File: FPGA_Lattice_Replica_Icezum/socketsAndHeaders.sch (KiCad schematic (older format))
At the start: 39 parts, among them J10 1x8_male_pin_Header_2.54mm, J11 1x6_female_pin_Header_2.54mm, J12 1x6_female_pin_Header_2.54mm, J13 1x6_female_pin_Header_2.54mm, J14 1x6_female_pin_Header_2.54mm, J19 2x4_male_pin_Header_2.54mm, J2 1x6_female_pin_Header_2.54mm, J3 1x6_female_pin_Header_2.54mm, J4 1x10_female_pin_Header_2.54mm, J5 1x8_male_pin_Header_2.54mm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

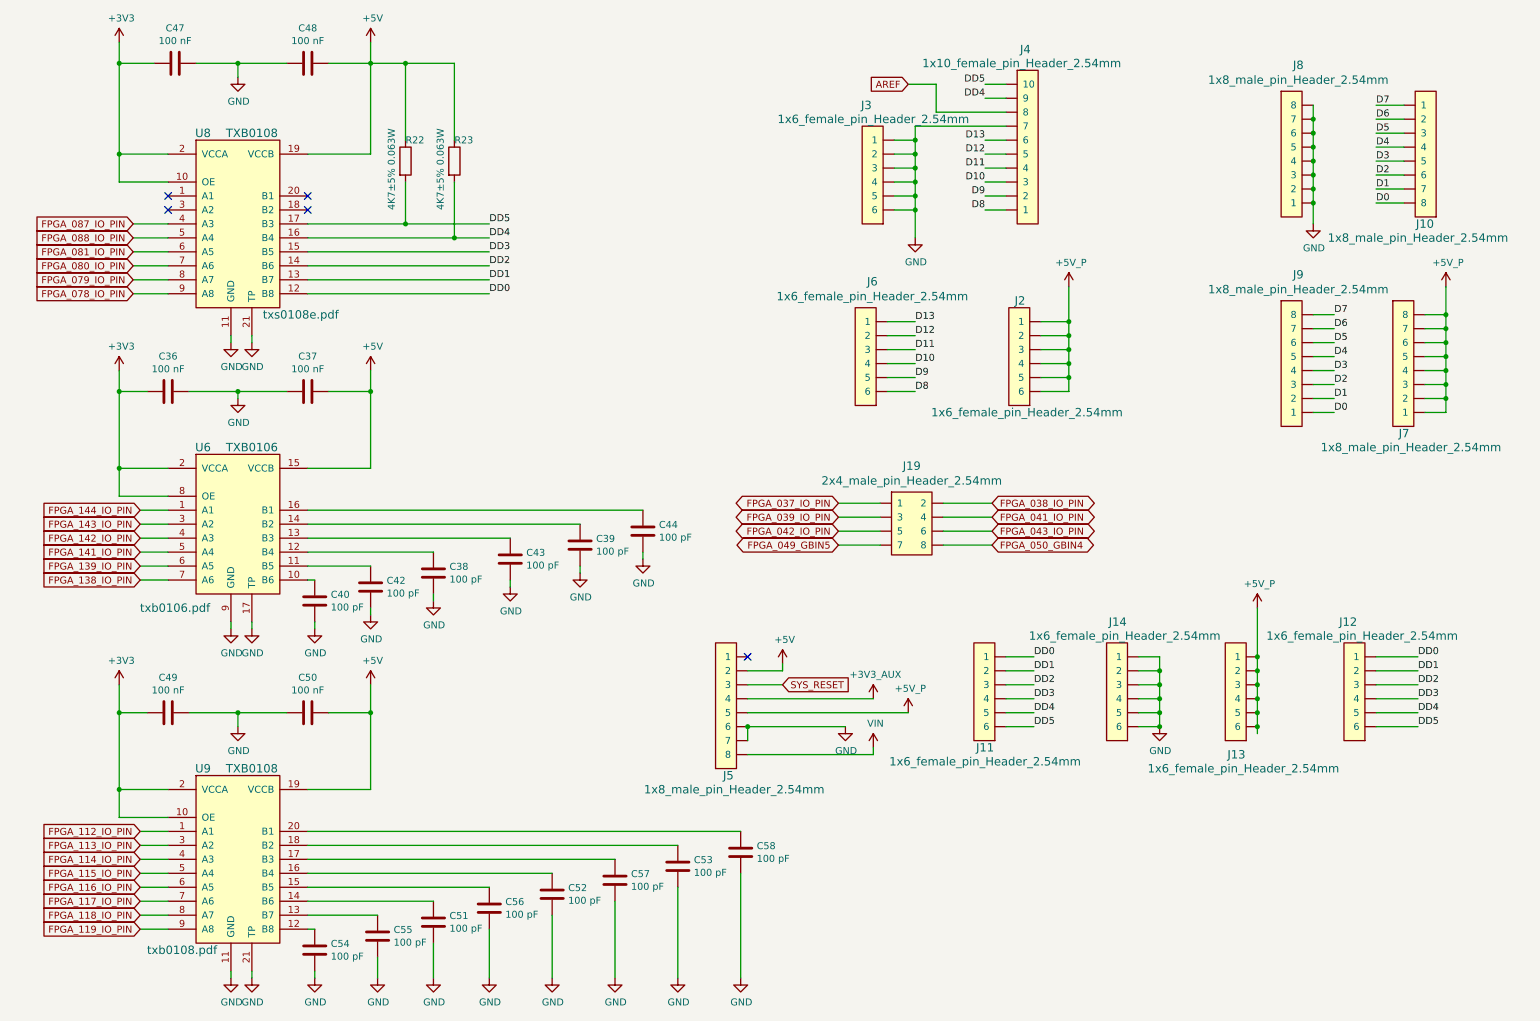
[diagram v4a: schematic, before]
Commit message: se realizo las correcciones sugeridas por el revisor
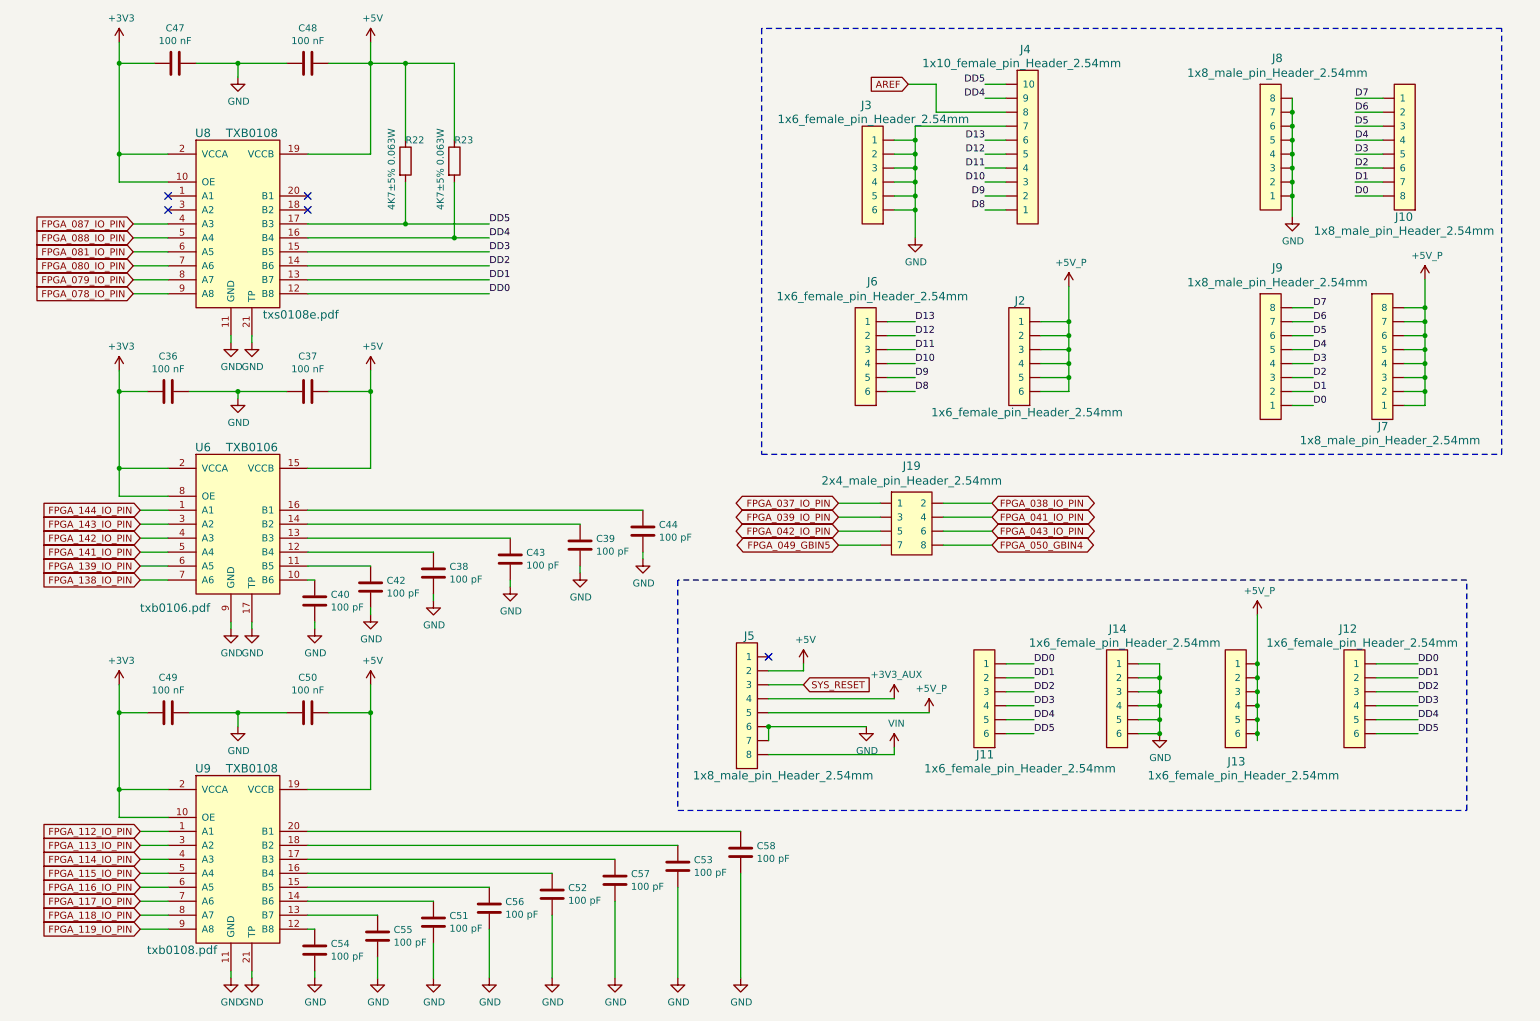
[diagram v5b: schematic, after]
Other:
- moved on the sheet: J10, J11, J12, J13, J14, J5, J7, J8, J9

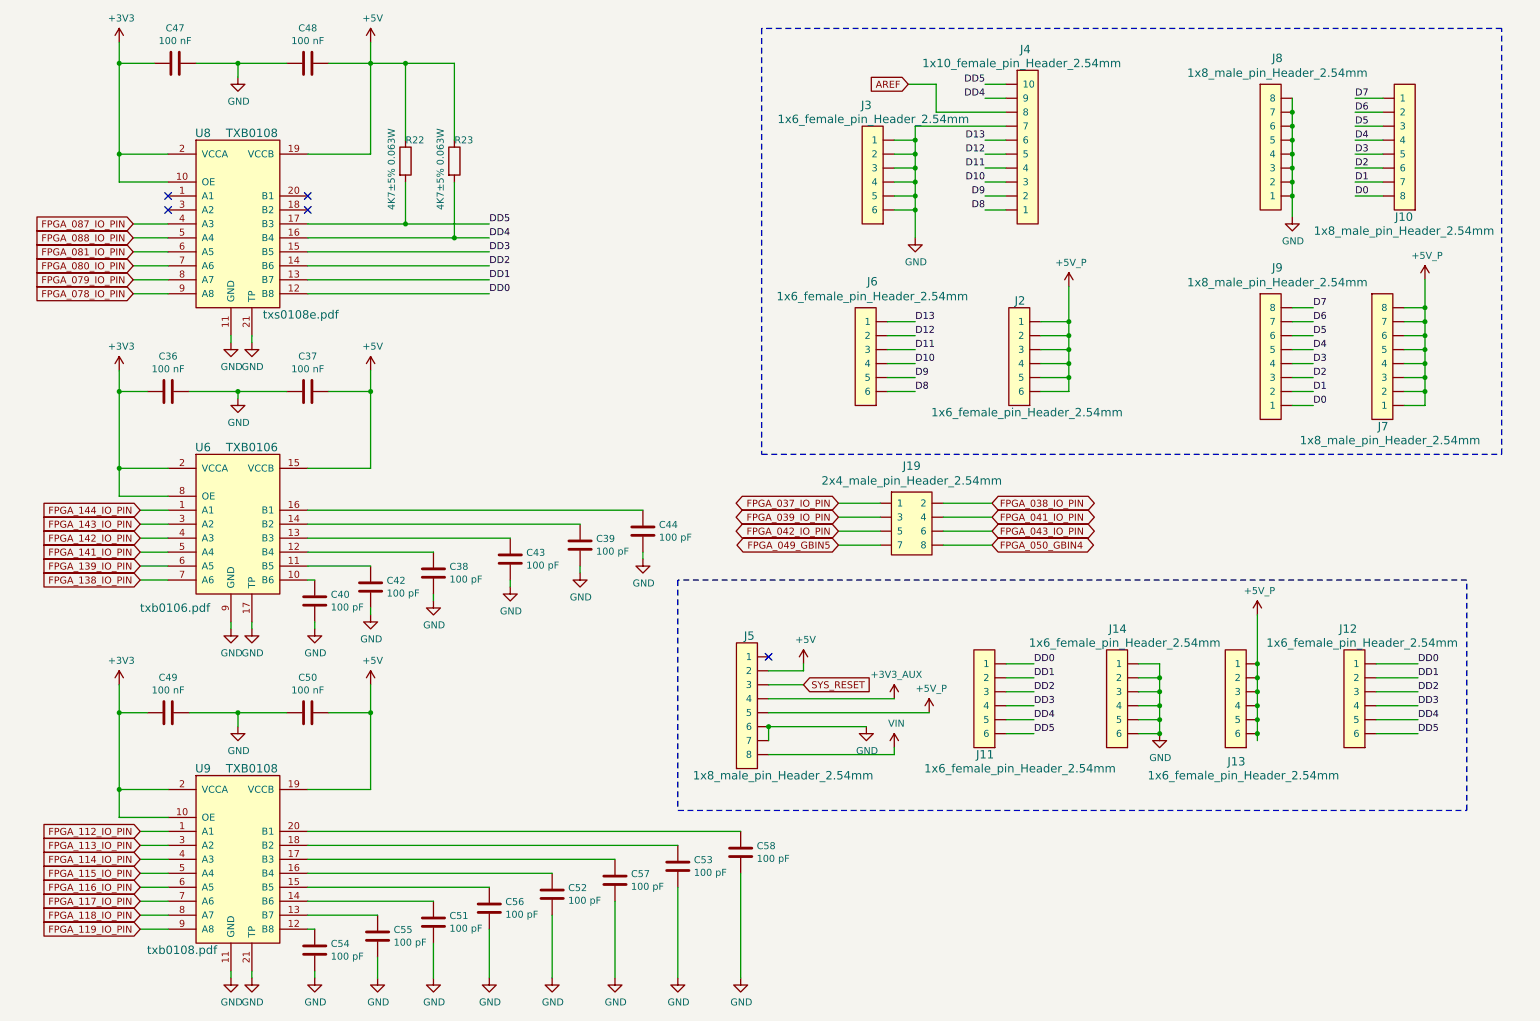
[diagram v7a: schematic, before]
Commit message: se mejoro esquematico de acuerdo a la revisión del docente. Se mejoro rotulo (se coloco link del repo, autor y autor de la versión original y la licencia) se mejoro el flujo izquiera derecha de los botones, se desplazo fiduciales a la página principal, se achico el esquematico en la parte de headers
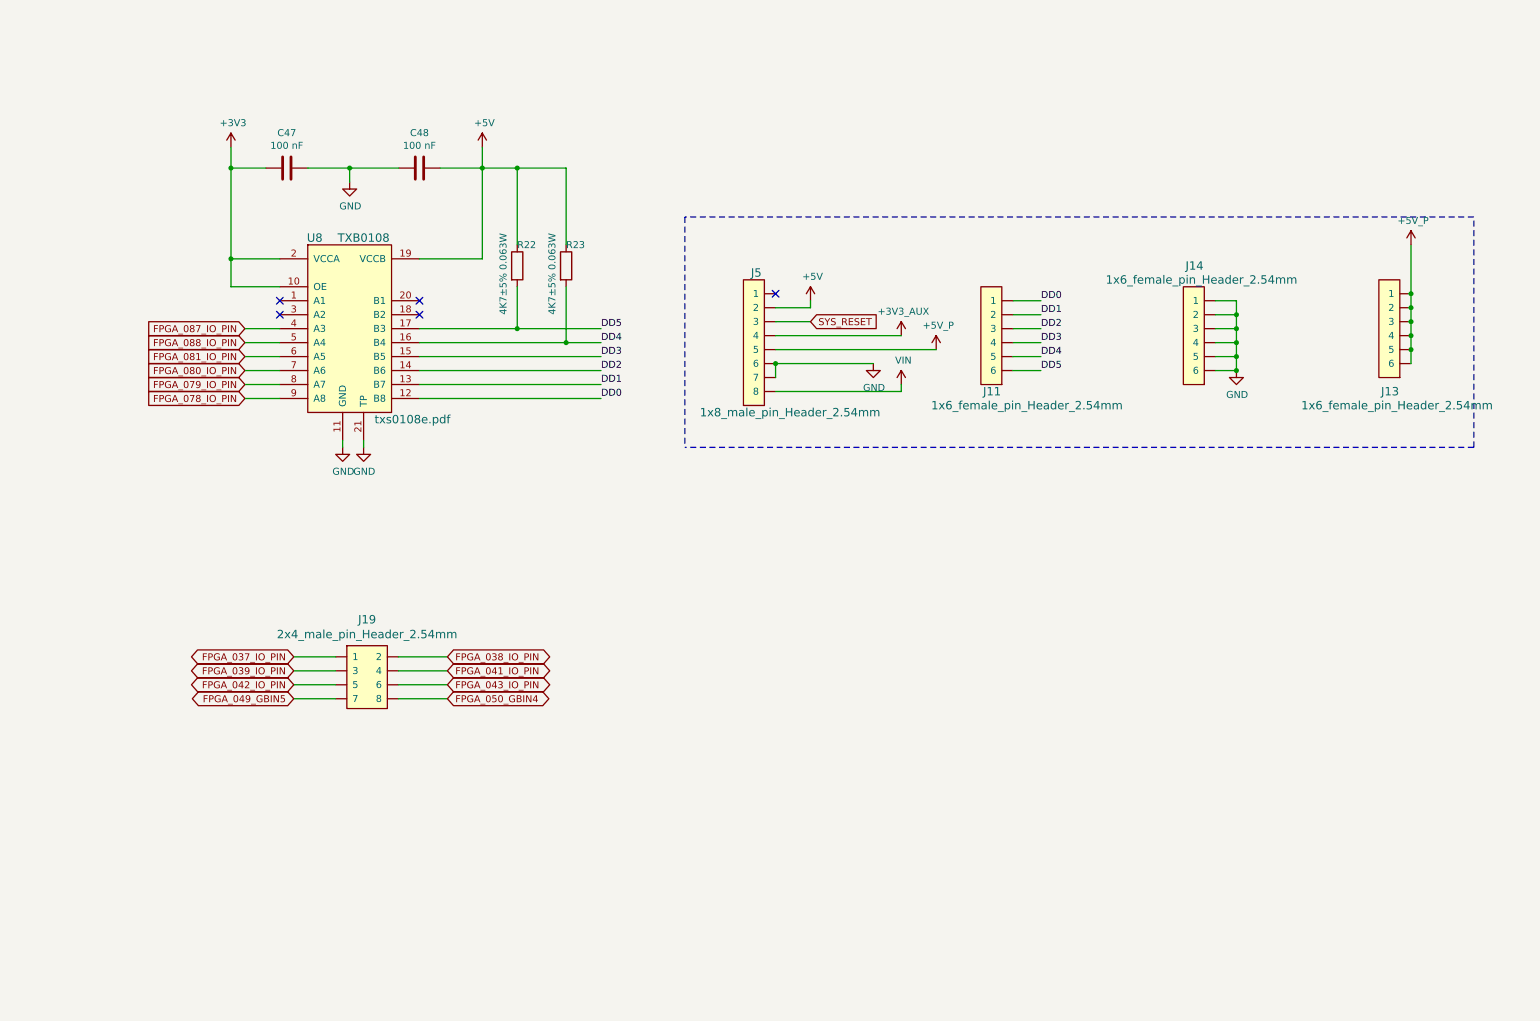
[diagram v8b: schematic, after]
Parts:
- removed C36, C37, C50: 100 nF, footprints:C_0402, symbol Device:C
- removed C38, C39, C40, C42, C43, C44, C51, C52, C53, C54, C55, C56, C57, C58: 100 pF, footprints:C_0402, symbol Device:C
- removed C49: 100 nF, footprints:C_0603, symbol Device:C
- removed J10, J7, J8, J9: 1x8_male_pin_Header_2.54mm, footprints:1x8_Socket_header_2.54mm, symbol icezum:1x8_male_pin_Header_2.54mm
- removed J12, J2, J3, J6: 1x6_female_pin_Header_2.54mm, footprints:1x6-pin-header-2.54mm, symbol icezum:1x6_female_pin_Header_2.54mm
- removed J4: 1x10_female_pin_Header_2.54mm, footprints:1x10_socket-header-2.54mm, symbol icezum:1x10_female_pin_Header_2.54mm
- removed U6: TXB0106, footprints:VQFN16, symbol icezum:TXB0106
- removed U9: TXB0108, footprints:VQFN20, symbol icezum:TXB0108
- C47, C48: footprint footprints:C_0402 -> footprints:L_0805
- R22, R23: footprint footprints:R_0402 -> footprints:F_0805
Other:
- moved on the sheet: C47, C48, J11, J13, J14, J19, J5, R22, R23, U8
